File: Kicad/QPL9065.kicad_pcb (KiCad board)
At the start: 4 copper layers, 30 x 30 mm, 24 parts, among them J1 Conn_Coaxial, J2 Conn_Coaxial, J3 Conn_Coaxial_Power, U1 QPL9065

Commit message: Shield line, new footprint, cleanup
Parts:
- U1: footprint Package_DFN_QFN:QFN-16-1EP_3x3mm_P0.5mm_EP2.7x2.7mm_ThermalVias -> Package_DFN_QFN:UQFN-16-1EP_3x3mm_P0.5mm_QPL9065
- moved C12 1.29 mm to (154.8, 85.5)
- moved C7 1.15 mm to (149.7, 88.2)
- moved L2 1.15 mm to (149.2, 90.8)
- moved C8 1.15 mm to (149.7, 89.2)
- moved R2 0.87 mm to (149.2, 86.7), turned to 270 degrees
- moved R1 0.76 mm to (155.2, 87.2), turned to 90 degrees
- moved L5 0.62 mm to (153.0, 91.0), turned to 0 degrees
- moved C6 0.46 mm to (155.7, 88.7)
- moved C5 0.18 mm to (155.7, 89.7)
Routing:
- net VDC: track 12.5 -> 13.1 mm
- net GND: vias 410 -> 419

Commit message: Case, Impedence matchine LNA
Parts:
- J1, J2: footprint Connector_Coaxial:SMA_Amphenol_132289_EdgeMount-RF -> Connector_Coaxial:‎142-1701-626‎
- J3: footprint Connector_Coaxial:SMA_Amphenol_132289_EdgeMount-RF -> Connector_Coaxial:132147-48
- moved J3 0.15 mm to (150.0, 81.5)
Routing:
- net /RFout: track 3.75 -> 5.90 mm
- net /RFin: track 6.04 -> 8.19 mm
- net GND: vias 419 -> 405
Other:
- outline, holes or cut-outs redrawn

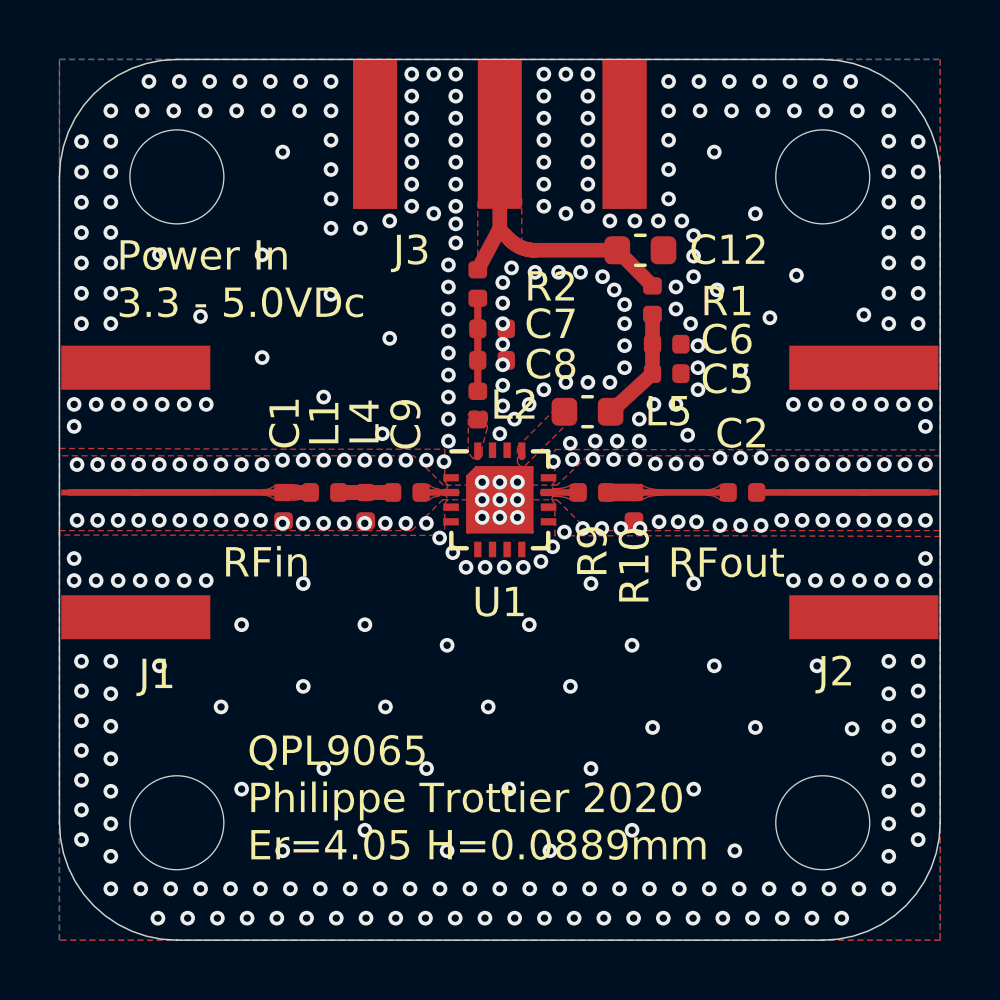
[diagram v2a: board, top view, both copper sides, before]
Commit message: QPL rework
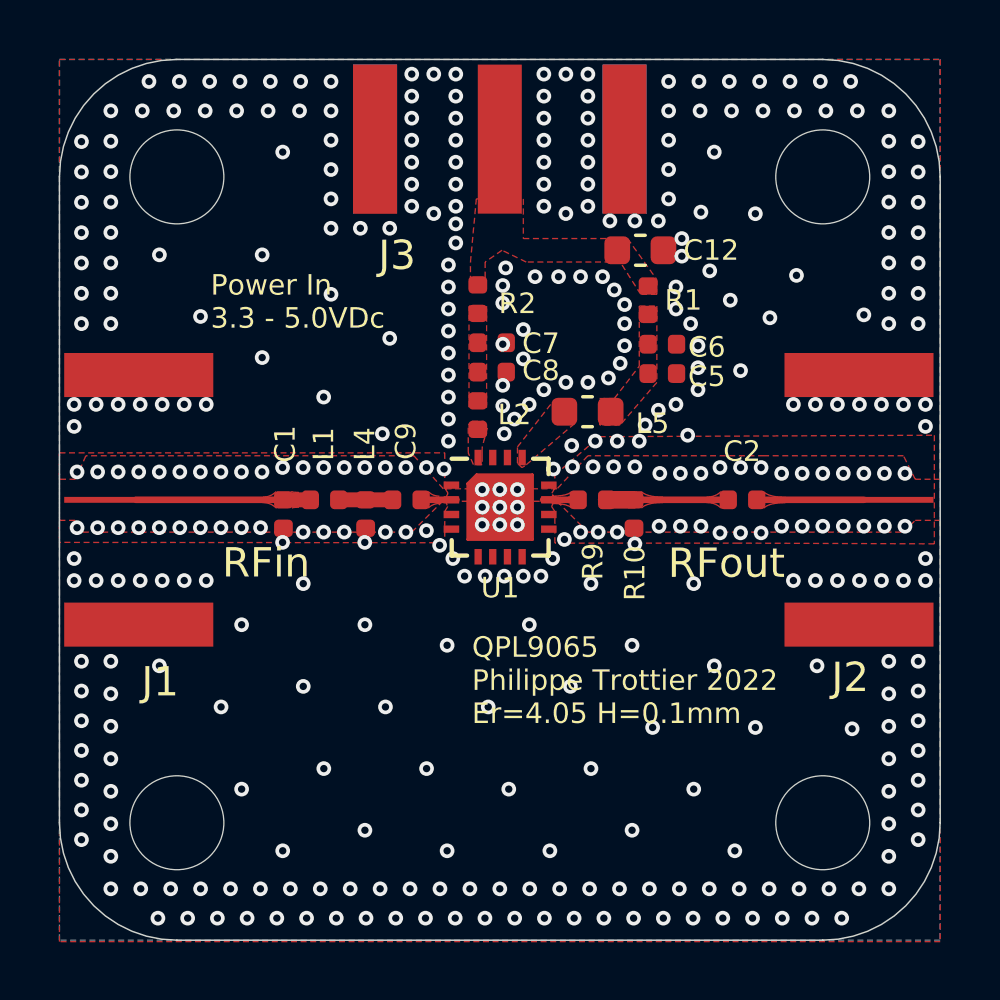
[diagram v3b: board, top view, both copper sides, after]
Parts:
- moved R2 0.52 mm to (149.2, 87.2)
- moved C7 0.48 mm to (149.7, 88.7)
- moved C8 0.40 mm to (149.7, 89.7)
- moved L2 0.32 mm to (149.2, 91.1)
- moved J2 0.30 mm to (162.2, 94.0)
- moved J1 0.27 mm to (137.7, 94.0)
- moved U1 0.25 mm to (150.0, 94.2)
- moved C1 0.25 mm to (142.6, 94.5)
- moved C2 0.25 mm to (158.3, 94.0)
- moved C9 0.25 mm to (146.8, 94.0)
- moved L1 0.25 mm to (144.0, 94.0)
- moved L4 0.25 mm to (145.4, 94.5)
- moved R10 0.25 mm to (154.6, 94.5)
- moved R9 0.25 mm to (153.2, 94.0)
- moved J3 0.17 mm to (150.0, 81.7)
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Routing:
- net VDC: track 13.1 -> 0.00 mm
- net Net-(C5-Pad1): track 3.94 -> 0.00 mm
- net Net-(C7-Pad1): track 3.17 -> 0.00 mm
- net /RFout: track 5.90 -> 3.65 mm
- net /RFin: track 8.19 -> 5.94 mm
- net GND: vias 405 -> 403
- added copper zone on F.Cu, net Net-(C5-Pad1)
- added copper zone on F.Cu, net Net-(C7-Pad1)
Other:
- net class Default removed
- board text added: "QPL9065 Philippe Trottier 2022 Er=4.05 H=0.1mm"
- board text removed: "QPL9065 Philippe Trottier 2020 Er=4.05 H=0.0889mm"
